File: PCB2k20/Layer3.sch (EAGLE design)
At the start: 11 parts, among them U1 TPS5430

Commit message: no idea what i did but need to save this so
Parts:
- removed C1: 22.0uF, JH:CAPACITOR1210
- removed C2: 4.7uF, JH:CAPACITOR0603
- removed C3: 220uF, rcl:CPOL-USD/7343-31R
- removed C4: 0.1uF, JH:CAPACITOR0603
- removed C5: 10.0nF, JH:CAPACITOR0603
- removed D1: 3A/40V/500mV, SparkFun-DiscreteSemi:DIODE-SCHOTTKY-B340A
- removed L1: SWPA8040/10uH, JH:INDUCTORSWPA8040
- removed U1: TPS5430, JH:TPS5450
- added 1C1, 1C11, 1C3, 1C4: 1uF, JH:CAPACITOR0603
- added 1C7, 1C8: 20pF, JH:CAPACITOR0603
- added 1D1: BLUE, SparkFun-LED:LED-BLUE0603
- added 1OSC: 8MHz, SparkFun-Clocks:CRYSTALSMD-5X3.2-2PAD
- added 1R1, 1R5: 1k, JH:RESISTOR0603
- added 1R4, 2R1, R3: 10k, JH:RESISTOR0603
- added 1S2: MOMENTARY_SWITCH_4X3, JH:MOMENTARY_SWITCH_4X3
- added 1U1: STM32F103CBT6, JH:STM32F103CBT6
- added 2C1: 22.0uF, JH:CAPACITOR1210
- added 2C2: 4.7uF, JH:CAPACITOR0603
- added 2C3: 10.0nF, JH:CAPACITOR0603
- added 2C4: 220uF, rcl:CPOL-USD/7343-31R
- added 2C5: 0.1uF, JH:CAPACITOR0603
- added 2D1: 3A/40V/500mV, SparkFun-DiscreteSemi:DIODE-SCHOTTKY-B340A
- added 2L1: SWPA8040/10uH, JH:INDUCTORSWPA8040
- added 2R2: 5.9k, JH:RESISTOR0603
- added 2U1: TPS5430, JH:TPS5450
- added AT_SELECT: CONN_03, JH:CONN_03
- added BATT_JN: XT60XT60PW-M, JH:XT60XT60PW-M
- added ESC1, ESC2: XT30PW-F, JH:XT30PW-F
- added HC05: (no value), SparkFun-Connectors:CONN_06RA_LOCK
- added IMU: (no value), SparkFun-Connectors:CONN_06FEMALE_LOCK
- added J5: (no value), SparkFun-Connectors:CONN_05LOCK
- added PCB1: RPI3, JH:RPI3
- added R6, R7: (no value), JH:RESISTOR0603
- added RPI_POWER, RPI_UART: (no value), SparkFun-Connectors:CONN_02LOCK
- added S1: DIP-04SMD, SparkFun-Switches:DIP-04SMD
- added S2: (no value), SparkFun-Switches:SWITCH-SPDT-PTH-11.6X4.0MM-LOCK
- added SWD: (no value), SparkFun-Connectors:CONN_04LOCK
- R1: value 10k -> 300k
- R2: value 3.24k -> 100k
- U$1: value TEENSY_3.5/3.6 -> TEENSY_3.5/3.6_NO_MIDDLE; device JH:TEENSY_3.5/3.6 -> JH:TEENSY_3.5/3.6_NO_MIDDLE
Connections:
- removed net N$1: R1.1, R2.2, U1.VSNS
- removed net N$2: C5.1, U1.BOOT
- removed net N$5: C5.2, D1.C, L1.1, U1.PH
- removed net VIN: C1.1, C2.1, U1.VIN
- removed net VOUT: C3.+, C4.1, L1.2, R1.2
- new net 12V: 2C1.1, 2C2.1, 2U1.VIN, BATT_JN.P$V+, ESC1.P$V+, ESC2.P$V+, R1.2
- new net 3.3V: 1C1.1, 1C11.1, 1C3.1, 1C4.1, 1R4.2, 1U1.VDD_1, 1U1.VDD_2, 1U1.VDD_3, 1U1.VDD_A, AT_SELECT.1, HC05.2, IMU.6, J5.4, R6.2, R7.2, SWD.4
- new net 33: 1R1.2, 1U1.PB1/ADC12_IN9/TIM3_CH4
- new net 5V: 2C4.+, 2C5.1, 2L1.2, 2R1.2, J5.5, S2.O, U$1.VIN
- new net BATT_LVL: R1.1, R2.1
- new net BT_KEY: AT_SELECT.2, HC05.1
- new net BT_RX: HC05.5
- new net BT_STATE: HC05.6
- new net BT_TX: HC05.4
- new net IMU_RST: IMU.1
- new net IMU_SCL: 1U1.PB6/I2C1_SCL/TIM4_CH1, IMU.3, R6.1
- new net IMU_SDA: 1U1.PB7/I2C1_SDA/TIM4_CH2, IMU.2, R7.1
- new net L3_RX: 1U1.PA10/USART1_RX/TIM1_CH3
- new net L3_TX: 1U1.PA9/USART1_TX/TIM1_CH2
- new net L4_RX: J5.2
- new net L4_TX: J5.3
- new net N$23: 1U1.BOOT0, R3.1
- new net N$3: 1D1.A, 1R1.1
- new net N$4: 1R5.2, 1S2.1
- new net N$6: 2C3.2, 2D1.C, 2L1.1, 2U1.PH
- new net N$7: 2R1.1, 2R2.2, 2U1.VSNS
- new net N$8: 2C3.1, 2U1.BOOT
- new net N$9: RPI_POWER.2, S2.P
- new net OSC_IN: 1C7.1, 1OSC.2, 1U1.PD0-OSC_IN
- new net OSC_OUT: 1C8.1, 1OSC.1, 1U1.PD1-OSC_OUT
- new net RESET: 1R4.1, 1S2.2, 1U1.NRST
- new net RPI_RX: RPI_UART.1, U$1.0/RX
- new net RPI_TX: RPI_UART.2, U$1.1/TX
- new net SWDCLK: 1U1.PA14/JTCK/SWCLK, SWD.2
- new net SWDIO: 1U1.PA13/JTMS/SWDIO, SWD.3
- net GND: now also 1C1.2, 1C11.2, 1C3.2, 1C4.2, 1C7.2, 1C8.2, 1D1.C, 1R5.1, 1U1.VSS_1, 1U1.VSS_2, 1U1.VSS_3, 1U1.VSS_A, 2C1.2, 2C2.2, 2C4.-, 2C5.2, 2D1.A, 2R2.1, 2U1.GND, AT_SELECT.3, BATT_JN.P$V-, ESC1.P$V-, ESC2.P$V-, HC05.3, IMU.4, J5.1, R2.2, R3.2, RPI_POWER.1, SWD.1, U$1.GND; no longer C1.2, C2.2, C3.-, C4.2, D1.A, R2.1, U1.GND
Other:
- note added: "use xh2.54 here"

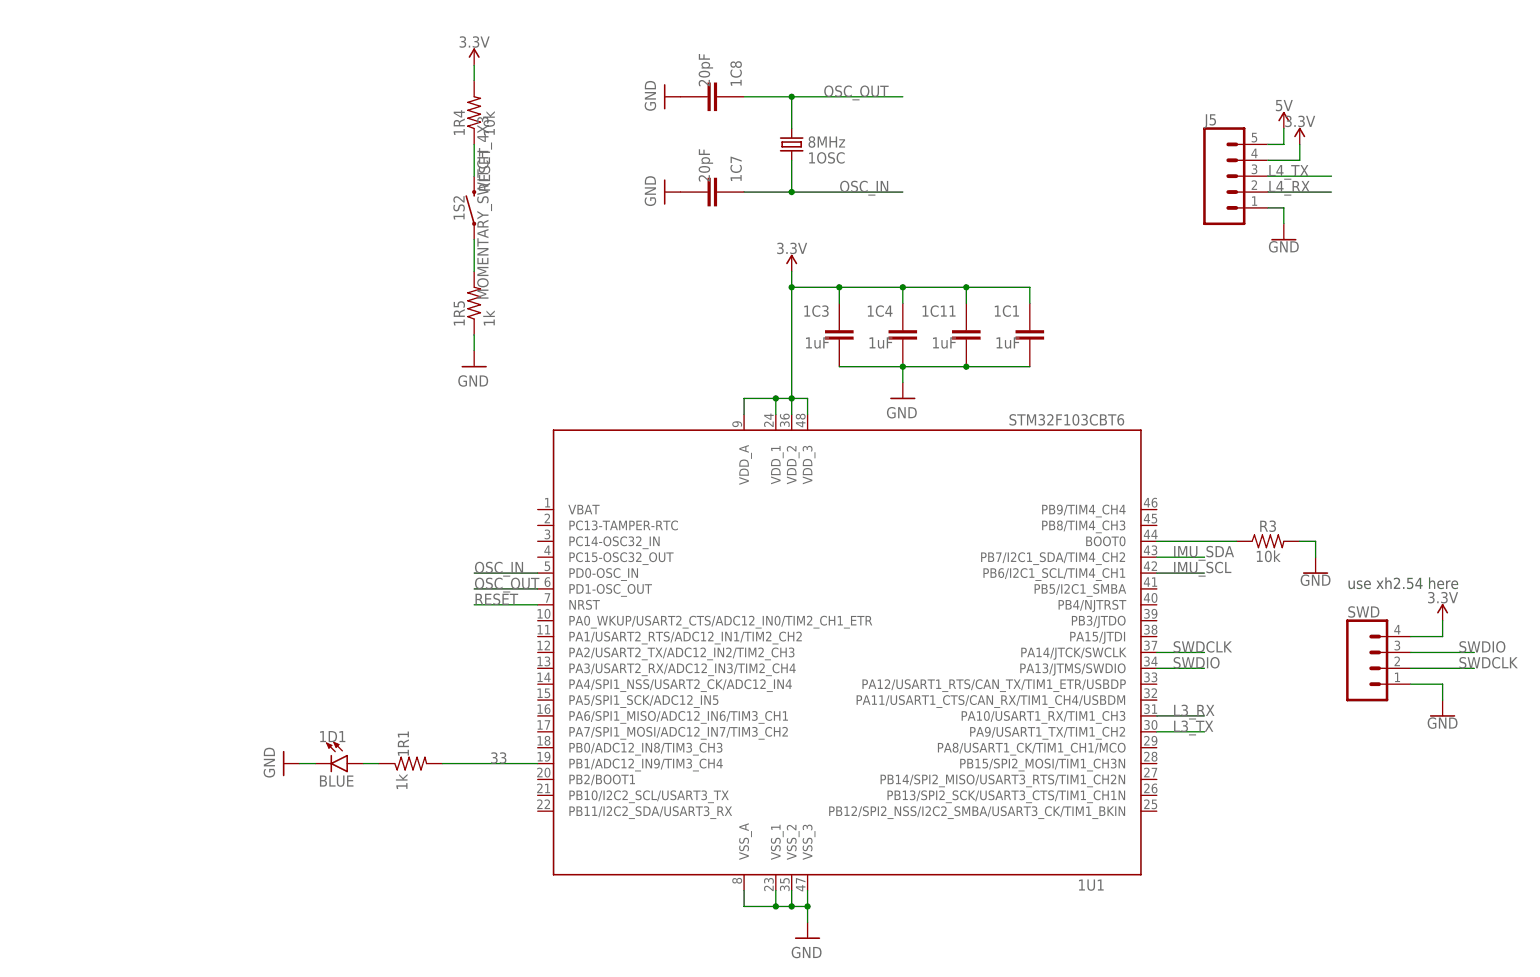
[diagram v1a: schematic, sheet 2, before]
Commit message: Layer 3 placement kinda done, routing to wait for layer 1 signals to be confirmed. also renamed some folders because windows explorer doesnt like the old name
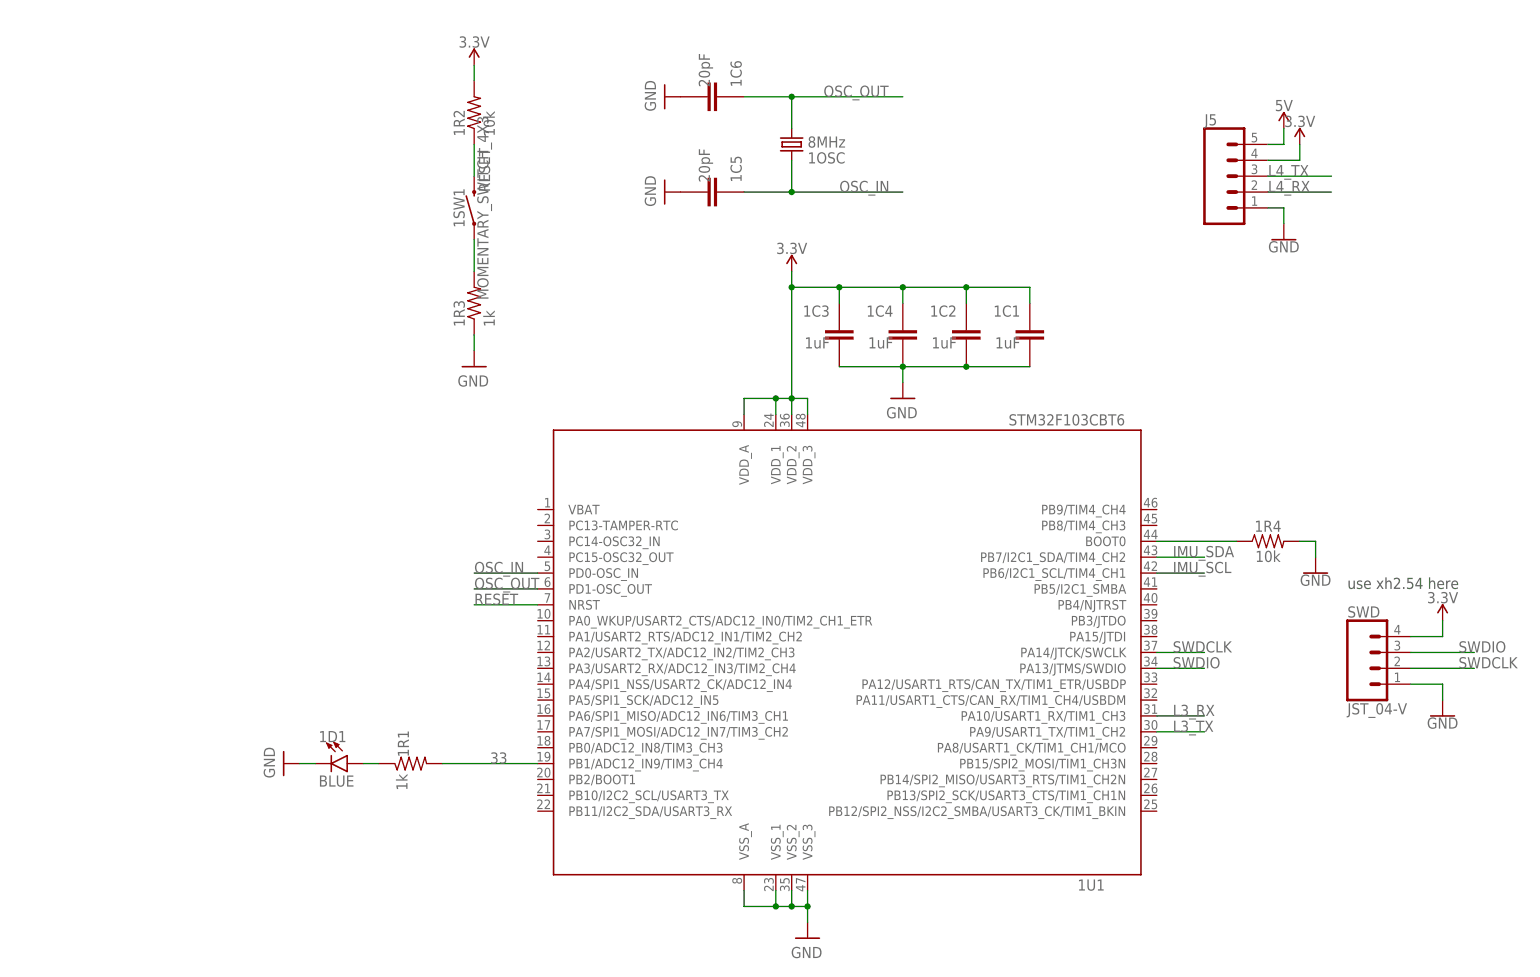
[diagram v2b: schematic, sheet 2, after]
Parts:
- removed R3: 10k, JH:RESISTOR0603
- added 1R2: 10k, JH:RESISTOR0603
- SWD: value (none) -> JST_04-V; device SparkFun-Connectors:CONN_04LOCK -> JH:JST_04-V
- renumbered 1C11 to 1C2, 1C7 to 1C5, 1C8 to 1C6, 1R5 to 1R3, 1S2 to 1SW1
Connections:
- net 3.3V: now also 1R2.2; no longer 1R4.2
- net GND: now also 1R4.2; no longer R3.2
- net N$23: now also 1R4.1; no longer R3.1
- net RESET: now also 1R2.1; no longer 1R4.1
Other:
- moved on the sheet: 1R4

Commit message: continue on layer 1 schematic, just need to finish this asap and quickly start positioning
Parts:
- added U$2: XT60XT60PW-F, JH:XT60XT60PW-F
- 2R2: value 5.9k -> 3.24k
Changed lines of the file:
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@@
 <drawing>
 <settings>
-<setting alwaysvectorfont="no"/>
+<setting alwaysvectorfont="yes"/>
 <setting verticaltext="up"/>
 </settings>
@@
 <part name="GND4" library="SparkFun-PowerSymbols" deviceset="GND" device=""/>
 <part name="2C5" library="JH" library_urn="urn:adsk.eagle:library:6027132" deviceset="CAPACITOR" device="0603" package3d_urn="urn:adsk.eagle:package:15441226/3" value="0.1uF"/>
-<part name="2R2" library="JH" library_urn="urn:adsk.eagle:library:6027132" deviceset="RESISTOR" device="0603" package3d_urn="urn:adsk.eagle:package:15441228/3" value="5.9k"/>
+<part name="2R2" library="JH" library_urn="urn:adsk.eagle:library:6027132" deviceset="RESISTOR" device="0603" package3d_urn="urn:adsk.eagle:package:15441228/3" value="3.24k"/>
 <part name="SUPPLY9" library="SparkFun-PowerSymbols" library_urn="urn:adsk.eagle:library:530" deviceset="12V" device=""/>
 <part name="SUPPLY10" library="SparkFun-PowerSymbols" library_urn="urn:adsk.eagle:library:530" deviceset="5V" device=""/>
@@
 <part name="GND3" library="SparkFun-PowerSymbols" library_urn="urn:adsk.eagle:library:530" deviceset="GND" device=""/>
 <part name="PCB1" library="JH" library_urn="urn:adsk.eagle:library:6027132" deviceset="RPI3" device="" package3d_urn="urn:adsk.eagle:package:9592022/2"/>
+<part name="U$2" library="JH" library_urn="urn:adsk.eagle:library:6027132" deviceset="XT60" device="XT60PW-F" package3d_urn="urn:adsk.eagle:package:16411181/4"/>
 </parts>
 <sheets>
@@
 </instance>
 <instance part="PCB1" gate="G$1" x="101.6" y="88.9" smashed="yes"/>
+<instance part="U$2" gate="G$1" x="182.88" y="45.72" smashed="yes">
+<attribute name="NAME" x="179.578" y="40.64" size="1.778" layer="95" font="vector" rot="R90"/>
+<attribute name="VALUE" x="187.96" y="40.64" size="1.778" layer="95" font="vector" rot="R90"/>
+</instance>
 </instances>
 <busses>

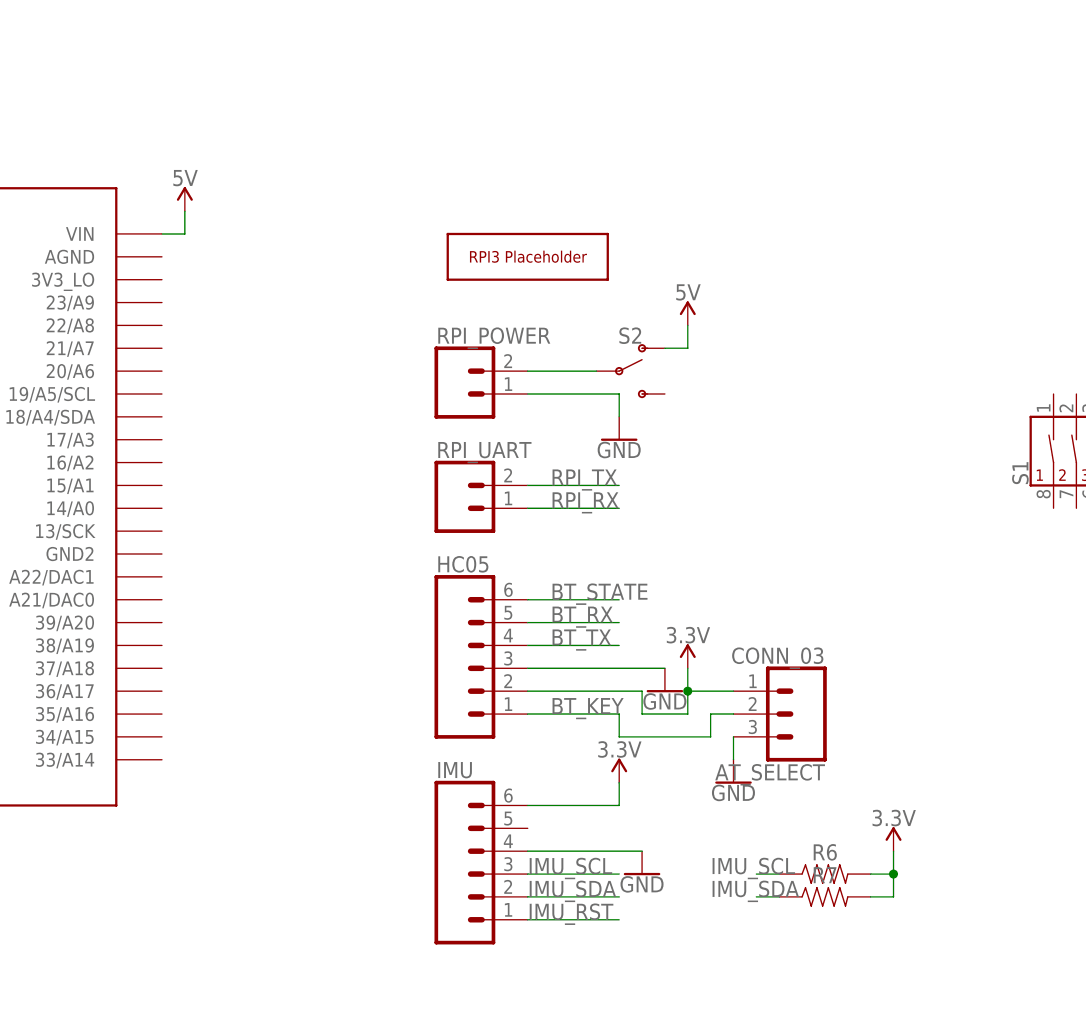
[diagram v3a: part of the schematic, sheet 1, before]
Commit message: added a switch to choose between programmer power and battery power for STM32
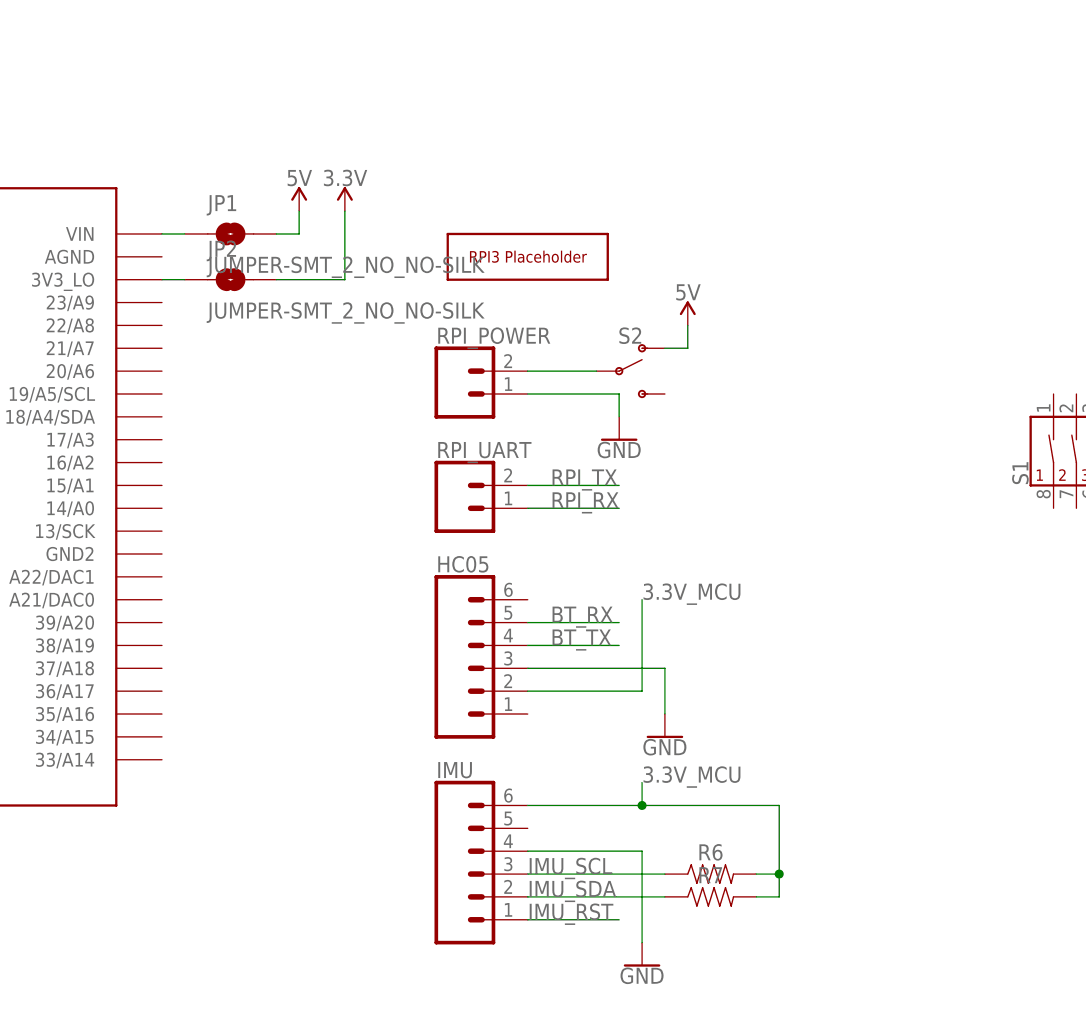
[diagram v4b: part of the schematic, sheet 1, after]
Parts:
- removed AT_SELECT: CONN_03, JH:CONN_03
- added JP1, JP2: JUMPER-SMT_2_NO_NO-SILK, SparkFun-Jumpers:JUMPER-SMT_2_NO_NO-SILK
- added S3: (no value), SparkFun-Switches:SWITCH-SPDT-PTH-11.6X4.0MM-LOCK
- SWD: value JST_04-V -> SM06B-SRSS-TB; device JH:JST_04-V -> con-JST SH:SM06B-SRSS-TB
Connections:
- removed net BT_KEY: AT_SELECT.2, HC05.1
- removed net BT_STATE: HC05.6
- new net 3.3V_MCU: 1C1.1, 1C2.1, 1C3.1, 1C4.1, 1R2.2, 1U1.VDD_1, 1U1.VDD_2, 1U1.VDD_3, 1U1.VDD_A, HC05.2, IMU.6, R6.2, R7.2, S3.P
- new net 3.3V_PROG: S3.S, SWD.4
- new net DEBUG_RX: 1U1.PA3/USART2_RX/ADC12_IN3/TIM2_CH4, SWD.6
- new net DEBUG_TX: 1U1.PA2/USART2_TX/ADC12_IN2/TIM2_CH3, SWD.5
- new net N$1: JP1.1, U$1.VIN
- new net N$2: JP2.1, U$1.3V3_LO
- net 3.3V: now also JP2.2, S3.O; no longer 1C1.1, 1C2.1, 1C3.1, 1C4.1, 1R2.2, 1U1.VDD_1, 1U1.VDD_2, 1U1.VDD_3, 1U1.VDD_A, AT_SELECT.1, HC05.2, IMU.6, R6.2, R7.2, SWD.4
- net 5V: now also JP1.2; no longer U$1.VIN
- net GND: no longer AT_SELECT.3
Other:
- note removed: "use xh2.54 here"
- moved on the sheet: 1C5, 1C6, 1OSC, R6, R7

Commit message: done just need to silkscreen now!!!
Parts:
- added J1, J3, J4, J6: 14AWG, JH:14AWG
- added J2: CONN_03, JH:CONN_03
- added R10, R3, R4, R5, R8, R9: (no value), JH:RESISTOR0603
- added X1: BM10B-SRSS-TB, con-JST SH:BM10B-SRSS-TB
- RPI_UART: device SparkFun-Connectors:CONN_02LOCK -> SparkFun-Connectors:CONN_06LOCK
- S1: value DIP-04SMD -> DIP-06; device SparkFun-Switches:DIP-04SMD -> SparkFun-Switches:DIP-06
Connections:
- new net INM1: U$1.A21/DAC0, X1.8
- new net INM2: U$1.A22/DAC1, X1.6
- new net INM3: U$1.13/SCK, X1.4
- new net INM4: U$1.14/A0, X1.2
- new net L1_RX: U$1.33/A14, X1.9
- new net L1_TX: U$1.34/A15, X1.10
- new net LIGHT_INT: J2.1, U$1.39/A20
- new net N$10: R3.1, S1.12, U$1.24
- new net N$11: R5.1, S1.10, U$1.26
- new net N$12: R8.1, S1.9, U$1.27
- new net N$5: R4.1, S1.11, U$1.25
- new net PWMM1: U$1.35/A16, X1.7
- new net PWMM2: U$1.36/A17, X1.5
- new net PWMM3: U$1.37/A18, X1.3
- new net PWMM4: U$1.38/A19, X1.1
- new net RPI_1: R10.1, RPI_UART.2, S1.7
- new net RPI_2: R9.1, RPI_UART.1, S1.8
- net 12V: now also J1.1, J3.1, U$2.P$V+
- net 3.3V: now also J2.3, R10.2, R3.2, R4.2, R5.2, R8.2, R9.2
- net BATT_LVL: now also U$1.15/A1
- net BT_RX: now also U$1.8
- net BT_TX: now also U$1.7
- net GND: now also J2.2, J4.1, J6.1, S1.1, S1.2, S1.3, S1.4, S1.5, S1.6, U$2.P$V-
- net L3_RX: now also U$1.1/TX
- net L3_TX: now also U$1.0/RX
- net L4_RX: now also U$1.10/CS
- net L4_TX: now also U$1.9/CS
- net RPI_RX: now also RPI_UART.5, U$1.32/A13; no longer RPI_UART.1, U$1.0/RX
- net RPI_TX: now also RPI_UART.6, U$1.31/A12; no longer RPI_UART.2, U$1.1/TX
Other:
- moved on the sheet: BATT_JN, ESC1, ESC2, HC05, IMU, JP1, JP2, R1, R2, R6, R7, RPI_POWER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
